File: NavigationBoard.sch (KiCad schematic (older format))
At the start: 13 parts, among them J1 Conn_01x03, J2 Conn_01x03, J3 Conn_01x03, J4 Conn_01x03, U1 ATmega2560-16AU, U2 RFM96W-433S2, U4 MPL115A1, U5 L86

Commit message: remove L86, fix Lora symbol
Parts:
- removed U5: L86, GPS:L86, symbol GPS:L86
- U2: symbol RF_AM_FM:RFM96W-433S2 -> RF_Module:RFM96W-433S2
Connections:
- wire segments 34 -> 27

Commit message: 3V regulator, crystal oscillator, reset switch, new GPS
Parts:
- added C10: 22µF, Capacitor_SMD:C_1206_3216Metric, symbol Device:C
- added C7, C8: 8pF, Capacitor_SMD:C_0603_1608Metric, symbol Device:C_Small
- added C9: 10µF, Capacitor_SMD:C_1210_3225Metric, symbol Device:C
- added R10, R11, R7, R8, R9: 10k, Resistor_SMD:R_0603_1608Metric, symbol Device:R_Small
- added SW1: SW_Push, Button_Switch_SMD:SW_SPST_PTS810, symbol Switch:SW_Push
- added U5: ublox_SAM-M8Q, RF_GPS:ublox_SAM-M8Q, symbol RF_GPS:ublox_SAM-M8Q
- added U6: LMZM23600V3, Package_LGA:Texas_SIL0010A_MicroSiP-10-1EP_3.8x3mm_P0.6mm_EP0.7x2.9mm_ThermalVias, symbol Regulator_Switching:LMZM23600V3
- added Y1: 16MHz, Crystal:Crystal_SMD_5032-2Pin_5.0x3.2mm, symbol Device:Crystal_Small
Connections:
- net labels added: +5V, ~RESET
- wire segments 27 -> 88
- no-connect marks 0 -> 1
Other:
- moved on the sheet: AE1, H1, H2, H3, H4, U1, U2

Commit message: add ISP, MPL3115A2
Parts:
- removed U4: MPL115A1, Package_LGA:NXP_MPL115A1_LGA-8_3x5mm_P1.25mm, symbol Sensor_Pressure:MPL115A1
- added J6: AVR-ISP-6, Connector_IDC:IDC-Header_2x03_P2.54mm_Vertical, symbol Connector:AVR-ISP-6
- added U4: MPL3115A2, Package_LGA:NXP_LGA-8_3x5mm_P1.25mm_H1.1mm, symbol Sensor_Pressure:MPL3115A2
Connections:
- net labels added: +3V3, ~RST
- wire segments 88 -> 94
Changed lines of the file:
@@
-$EndComp
-$Comp
-L Sensor_Pressure:MPL115A1 U4
-U 1 1 5CBD9B8B
-P 9700 4500
-F 0 "U4" H 10244 4546 50  0000 L CNN
-F 1 "MPL115A1" H 10244 4455 50  0000 L CNN
-F 2 "Package_LGA:NXP_MPL115A1_LGA-8_3x5mm_P1.25mm" H 9850 3800 50  0001 C CNN
-F 3 "http://www.nxp.com/assets/documents/data/en/data-sheets/MPL115A1.pdf" H 9700 4500 50  0001 C CNN
-	1    9700 4500
-	1    0    0    -1
 $EndComp
 $Comp
@@
 Wire Wire Line
 	6400 5500 6650 5500
+$Comp
+L Connector:AVR-ISP-6 J6
+U 1 1 5E8952E8
+P 6550 3800
+F 0 "J6" H 6270 3896 50  0000 R CNN
+F 1 "AVR-ISP-6" H 6270 3805 50  0000 R CNN
+F 2 "Connector_IDC:IDC-Header_2x03_P2.54mm_Vertical" V 6300 3850 50  0001 C CNN
+F 3 " ~" H 5275 3250 50  0001 C CNN
+	1    6550 3800
+	-1   0    0    -1
+$EndComp
+Wire Wire Line
+	6150 3600 6100 3600
+Wire Wire Line
+	6150 3700 6100 3700
+Wire Wire Line
+	6150 3800 6100 3800
+Wire Wire Line
+	6150 3900 6100 3900
+Wire Wire Line
+	6650 3300 6650 3200
+Wire Wire Line
+	6650 4200 6650 4300
+$Comp
+L power:GND #PWR0120
+U 1 1 5E8A7489
+P 6650 4300
+F 0 "#PWR0120" H 6650 4050 50  0001 C CNN
+F 1 "GND" H 6655 4127 50  0000 C CNN
+F 2 "" H 6650 4300 50  0001 C CNN
+F 3 "" H 6650 4300 50  0001 C CNN
+	1    6650 4300
+	1    0    0    -1
+$EndComp
+$Comp
+L power:+3V3 #PWR0121
+U 1 1 5E8A80F1
+P 6650 3200
+F 0 "#PWR0121" H 6650 3050 50  0001 C CNN
+F 1 "+3V3" H 6665 3373 50  0000 C CNN
+F 2 "" H 6650 3200 50  0001 C CNN
+F 3 "" H 6650 3200 50  0001 C CNN
+	1    6650 3200
+	1    0    0    -1
+$EndComp
+Text Label 6100 3600 2    50   ~ 0
+MISO
+Text Label 6100 3700 2    50   ~ 0
+MOSI
+Text Label 6100 3800 2    50   ~ 0
+SCK
+Text Label 6100 3900 2    50   ~ 0
+~RST
+$Comp
+L Sensor_Pressure:MPL3115A2 U4
+U 1 1 5E8CB1FC
+P 9650 4500
+F 0 "U4" H 9650 3911 50  0000 C CNN
+F 1 "MPL3115A2" H 9650 3820 50  0000 C CNN
+F 2 "Package_LGA:NXP_LGA-8_3x5mm_P1.25mm_H1.1mm" H 10650 4050 50  0001 C CNN
+F 3 "https://www.nxp.com/docs/en/data-sheet/MPL3115A2.pdf" H 9650 4500 50  0001 C CNN
+	1    9650 4500
+	1    0    0    -1
+$EndComp
 $EndSCHEMATC

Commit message: no clue, this has been >4 months and diff is kinda useless here...
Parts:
- added C11: 10µF, Capacitor_SMD:C_0603_1608Metric, symbol Device:C_Small
- added C12: 100nF, Capacitor_SMD:C_0603_1608Metric, symbol Device:C
- added C13: 100nF, Capacitor_SMD:C_0603_1608Metric, symbol Device:C_Small
- added J7: Conn_01x02, Connector_AMASS:AMASS_XT30UPB-M_1x02_P5.0mm_Vertical, symbol Connector_Generic:Conn_01x02
- added R12, R13: 10k, Resistor_SMD:R_0603_1608Metric, symbol Device:R_Small
- AE1: footprint Connector_Coaxial:MMCX_Molex_73415-0961_Horizontal_1.6mm-PCB -> Connector_Coaxial:SMA_Molex_73251-1153_EdgeMount_Horizontal
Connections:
- net +3V3: now also U4.1 (VDD), U4.4 (VDDIO), C11.2, C13.2, R12.1, R13.1
- net GND: now also C10.2, C9.2, U4.3 (GND), U6.1 (GND), U6.11 (GND), U6.2 (MODE/SYNC), C11.1, C12.1, C13.1
- net SCL: now reaches U1.43 (PD0)
- net SCL: now also U4.8 (SCL), R12.2
- net SDA: now reaches U1.44 (PD1)
- net SDA: now also U4.7 (SDL), R13.2
- net at U4.2 (CAP): now also C12.2
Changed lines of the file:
@@
 F 0 "AE1" H 6294 1989 50  0000 L CNN
 F 1 "Antenna_Shield" H 6294 1898 50  0000 L CNN
-F 2 "Connector_Coaxial:MMCX_Molex_73415-0961_Horizontal_1.6mm-PCB" H 6150 2050 50  0001 C CNN
+F 2 "Connector_Coaxial:SMA_Molex_73251-1153_EdgeMount_Horizontal" H 6150 2050 50  0001 C CNN
 F 3 "~" H 6150 2050 50  0001 C CNN
 	1    6150 1950
@@
 U 1 1 5CBDAC91
 P 5500 2500
-F 0 "U2" H 5500 3181 50  0000 C CNN
-F 1 "RFM96W-433S2" H 5500 3090 50  0000 C CNN
+F 0 "U2" H 5200 3000 50  0000 C CNN
+F 1 "RFM96W-433S2" H 5800 2950 50  0000 C CNN
 F 2 "RF_Module:HOPERF_RFM9XW_SMD" H 2200 4150 50  0001 C CNN
 F 3 "http://www.hoperf.com/upload/rf/RFM95_96_97_98W.pdf" H 2200 4150 50  0001 C CNN
@@
 U 1 1 5E8952E8
 P 6550 3800
-F 0 "J6" H 6270 3896 50  0000 R CNN
-F 1 "AVR-ISP-6" H 6270 3805 50  0000 R CNN
+F 0 "J6" H 6350 3450 50  0000 R CNN
+F 1 "AVR-ISP-6" H 7000 3450 50  0000 R CNN
 F 2 "Connector_IDC:IDC-Header_2x03_P2.54mm_Vertical" V 6300 3850 50  0001 C CNN
 F 3 " ~" H 5275 3250 50  0001 C CNN
@@
 U 1 1 5E8CB1FC
 P 9650 4500
-F 0 "U4" H 9650 3911 50  0000 C CNN
-F 1 "MPL3115A2" H 9650 3820 50  0000 C CNN
+F 0 "U4" H 9400 4050 50  0000 C CNN
+F 1 "MPL3115A2" H 10000 4050 50  0000 C CNN
 F 2 "Package_LGA:NXP_LGA-8_3x5mm_P1.25mm_H1.1mm" H 10650 4050 50  0001 C CNN
 F 3 "https://www.nxp.com/docs/en/data-sheet/MPL3115A2.pdf" H 9650 4500 50  0001 C CNN
@@
 	1    0    0    -1
 $EndComp
+Text Label 4650 3900 0    50   ~ 0
+SCL
+Text Label 4650 4000 0    50   ~ 0
+SDA
+$Comp
+L Device:R_Small R12
+U 1 1 5E8D9BD0
+P 4850 3700
+F 0 "R12" V 4850 3700 50  0000 C CNN
+F 1 "10k" V 4750 3700 50  0000 C CNN
+F 2 "Resistor_SMD:R_0603_1608Metric" H 4850 3700 50  0001 C CNN
+F 3 "~" H 4850 3700 50  0001 C CNN
+	1    4850 3700
+	1    0    0    -1
+$EndComp
+$Comp
+L Device:R_Small R13
+U 1 1 5E8D9BD6
+P 5000 3700
+F 0 "R13" V 5000 3700 50  0000 C CNN
+F 1 "10k" H 5059 3745 50  0001 L CNN
+F 2 "Resistor_SMD:R_0603_1608Metric" H 5000 3700 50  0001 C CNN
+F 3 "~" H 5000 3700 50  0001 C CNN
+	1    5000 3700
+	1    0    0    -1
+$EndComp
+$Comp
+L power:+3.3V #PWR0122
+U 1 1 5E8D9BDC
+P 4850 3500
+F 0 "#PWR0122" H 4850 3350 50  0001 C CNN
+F 1 "+3.3V" H 4865 3673 50  0000 C CNN
+F 2 "" H 4850 3500 50  0001 C CNN
+F 3 "" H 4850 3500 50  0001 C CNN
+	1    4850 3500
+	1    0    0    -1
+$EndComp
+Wire Wire Line
+	4850 3500 4850 3550
+Wire Wire Line
+	5000 3600 5000 3550
+Wire Wire Line
+	5000 3550 4850 3550
+Connection ~ 4850 3550
+Wire Wire Line
+	4850 3550 4850 3600
+Wire Wire Line
+	4850 3900 4850 3800
+Wire Wire Line
+	4550 3900 4850 3900
+Wire Wire Line
+	5000 4000 5000 3800
+Wire Wire Line
+	4550 4000 5000 4000
+Wire Wire Line
+	9250 4500 9150 4500
+Wire Wire Line
+	9250 4400 9150 4400
+Text Label 9150 4400 2    50   ~ 0
+SDA
+Text Label 9150 4500 2    50   ~ 0
+SCL
+Wire Wire Line
+	9550 4000 9550 3950
+Wire Wire Line
+	9550 3950 9650 3950
+Wire Wire Line
+	9650 3950 9650 4000
+Connection ~ 9550 3950
+Wire Wire Line
+	9550 3950 9550 3900
+$Comp
+L power:+3V3 #PWR0123
+U 1 1 5E8EE8BA
+P 9550 3900
+F 0 "#PWR0123" H 9550 3750 50  0001 C CNN
+F 1 "+3V3" H 9565 4073 50  0000 C CNN
+F 2 "" H 9550 3900 50  0001 C CNN
+F 3 "" H 9550 3900 50  0001 C CNN
+	1    9550 3900
+	1    0    0    -1
+$EndComp
+$Comp
+L power:GND #PWR0124
+U 1 1 5E8F05AB
+P 7200 5600
+F 0 "#PWR0124" H 7200 5350 50  0001 C CNN
+F 1 "GND" H 7205 5427 50  0000 C CNN
+F 2 "" H 7200 5600 50  0001 C CNN
+F 3 "" H 7200 5600 50  0001 C CNN
+	1    7200 5600
+	1    0    0    -1
+$EndComp
+Wire Wire Line
+	7200 5600 7200 5500
+$Comp
+L power:GND #PWR0125
+U 1 1 5E8F3C9C
+P 9650 5100
+F 0 "#PWR0125" H 9650 4850 50  0001 C CNN
+F 1 "GND" H 9655 4927 50  0000 C CNN
+F 2 "" H 9650 5100 50  0001 C CNN
+F 3 "" H 9650 5100 50  0001 C CNN
+	1    9650 5100
+	1    0    0    -1
+$EndComp
+Wire Wire Line
+	9650 5100 9650 5000
+$Comp
+L Device:C C12
+U 1 1 5E8F7F8C
+P 10300 4700
+F 0 "C12" V 10048 4700 50  0000 C CNN
+F 1 "100nF" V 10139 4700 50  0000 C CNN
+F 2 "Capacitor_SMD:C_0603_1608Metric" H 10338 4550 50  0001 C CNN
+F 3 "~" H 10300 4700 50  0001 C CNN
+	1    10300 4700
+	0    1    1    0
+$EndComp
+Wire Wire Line
+	10450 4700 10550 4700
+Wire Wire Line
+	10550 4700 10550 4800
+$Comp
+L power:GND #PWR0126
+U 1 1 5E8FB81C
+P 10550 4800
+F 0 "#PWR0126" H 10550 4550 50  0001 C CNN
+F 1 "GND" H 10555 4627 50  0000 C CNN
+F 2 "" H 10550 4800 50  0001 C CNN
+F 3 "" H 10550 4800 50  0001 C CNN
+	1    10550 4800
+	1    0    0    -1
+$EndComp
+Wire Wire Line
+	10150 4700 10050 4700
+$Comp
+L Device:C_Small C13
+U 1 1 5E8FF505
+P 10550 4100
+F 0 "C13" H 10458 4054 50  0000 R CNN
+F 1 "100nF" H 10458 4145 50  0000 R CNN
+F 2 "Capacitor_SMD:C_0603_1608Metric" H 10550 4100 50  0001 C CNN
+F 3 "~" H 10550 4100 50  0001 C CNN
+	1    10550 4100
+	-1   0    0    1
+$EndComp
+$Comp
+L Device:C_Small C11
+U 1 1 5E9000AF
+P 10200 4100
+F 0 "C11" H 10108 4054 50  0000 R CNN
+F 1 "10µF" H 10108 4145 50  0000 R CNN
+F 2 "Capacitor_SMD:C_0603_1608Metric" H 10200 4100 50  0001 C CNN
+F 3 "~" H 10200 4100 50  0001 C CNN
+	1    10200 4100
+	-1   0    0    1
+$EndComp
+Connection ~ 9650 3950
+Wire Wire Line
+	10200 4000 10200 3950
+Wire Wire Line
+	10200 3950 9650 3950
+Wire Wire Line
+	10200 4200 10200 4250
+Wire Wire Line
+	10200 4250 10550 4250
+Wire Wire Line
+	10550 4700 10550 4250
+Connection ~ 10550 4700
+Wire Wire Line
+	10550 4200 10550 4250
+Connection ~ 10550 4250
+Wire Wire Line
+	10200 3950 10550 3950
+Wire Wire Line
+	10550 3950 10550 4000
+Connection ~ 10200 3950
+$Comp
+L Connector_Generic:Conn_01x02 J7
+U 1 1 5E831A29
+P 8450 2750
+F 0 "J7" H 8530 2742 50  0000 L CNN
+F 1 "Conn_01x02" H 8530 2651 50  0000 L CNN
+F 2 "Connector_AMASS:AMASS_XT30UPB-M_1x02_P5.0mm_Vertical" H 8450 2750 50  0001 C CNN
+F 3 "~" H 8450 2750 50  0001 C CNN
+	1    8450 2750
+	1    0    0    -1
+$EndComp

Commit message: Erster Grober Entwurf
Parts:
- U4: symbol Sensor_Pressure:MPL3115A2 -> NavigationBoard-rescue:MPL3115A2-Sensor_Pressure
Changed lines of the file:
@@
 ~RST
 $Comp
-L Sensor_Pressure:MPL3115A2 U4
+L NavigationBoard-rescue:MPL3115A2-Sensor_Pressure U4
 U 1 1 5E8CB1FC
 P 9650 4500

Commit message: Kleinerer AVR-ISP Stecker
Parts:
- J6: footprint Connector_IDC:IDC-Header_2x03_P2.54mm_Vertical -> Connector_PinHeader_2.54mm:PinHeader_2x03_P2.54mm_Vertical
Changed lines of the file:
@@
 F 0 "J6" H 6350 3450 50  0000 R CNN
 F 1 "AVR-ISP-6" H 7000 3450 50  0000 R CNN
-F 2 "Connector_IDC:IDC-Header_2x03_P2.54mm_Vertical" V 6300 3850 50  0001 C CNN
+F 2 "Connector_PinHeader_2.54mm:PinHeader_2x03_P2.54mm_Vertical" V 6300 3850 50  0001 C CNN
 F 3 " ~" H 5275 3250 50  0001 C CNN
 	1    6550 3800

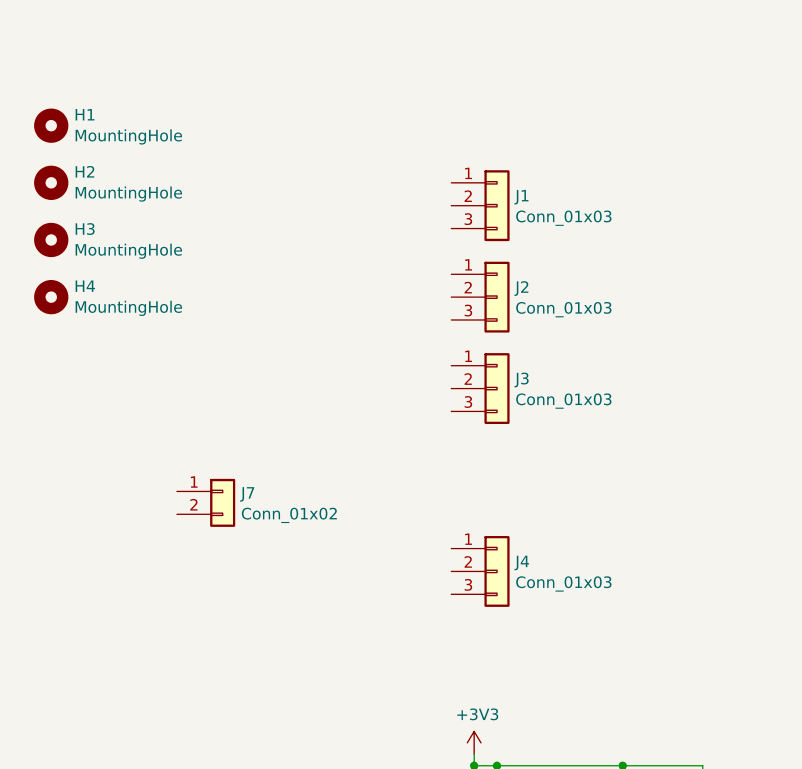
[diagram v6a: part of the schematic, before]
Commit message: XT 30 entfernt
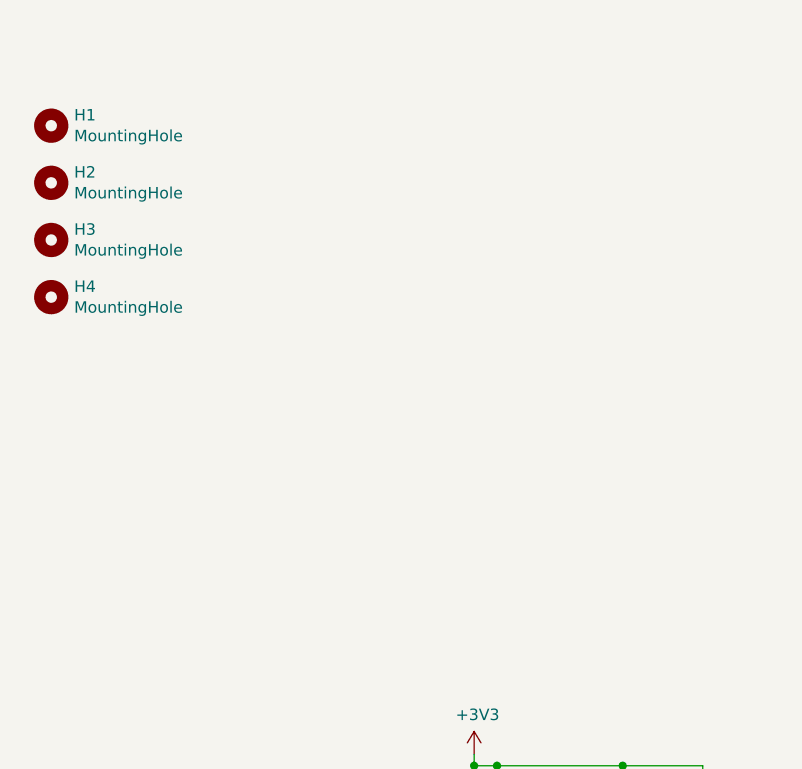
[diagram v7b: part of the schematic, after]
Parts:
- removed J1, J2, J3, J4: Conn_01x03, Connector_PinHeader_2.54mm:PinHeader_1x03_P2.54mm_Vertical, symbol Connector_Generic:Conn_01x03
- removed J7: Conn_01x02, Connector_AMASS:AMASS_XT30UPB-M_1x02_P5.0mm_Vertical, symbol Connector_Generic:Conn_01x02
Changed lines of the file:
@@
-$EndComp
-$Comp
-L Connector_Generic:Conn_01x03 J1
-U 1 1 5CBD6E70
-P 9650 1500
-F 0 "J1" H 9730 1542 50  0000 L CNN
-F 1 "Conn_01x03" H 9730 1451 50  0000 L CNN
-F 2 "Connector_PinHeader_2.54mm:PinHeader_1x03_P2.54mm_Vertical" H 9650 1500 50  0001 C CNN
-F 3 "~" H 9650 1500 50  0001 C CNN
-	1    9650 1500
-	1    0    0    -1
-$EndComp
-$Comp
-L Connector_Generic:Conn_01x03 J2
-U 1 1 5CBD7518
-P 9650 1900
-F 0 "J2" H 9730 1942 50  0000 L CNN
-F 1 "Conn_01x03" H 9730 1851 50  0000 L CNN
-F 2 "Connector_PinHeader_2.54mm:PinHeader_1x03_P2.54mm_Vertical" H 9650 1900 50  0001 C CNN
-F 3 "~" H 9650 1900 50  0001 C CNN
-	1    9650 1900
-	1    0    0    -1
-$EndComp
-$Comp
-L Connector_Generic:Conn_01x03 J3
-U 1 1 5CBD7CD8
-P 9650 2300
-F 0 "J3" H 9730 2342 50  0000 L CNN
-F 1 "Conn_01x03" H 9730 2251 50  0000 L CNN
-F 2 "Connector_PinHeader_2.54mm:PinHeader_1x03_P2.54mm_Vertical" H 9650 2300 50  0001 C CNN
-F 3 "~" H 9650 2300 50  0001 C CNN
-	1    9650 2300
-	1    0    0    -1
-$EndComp
-$Comp
-L Connector_Generic:Conn_01x03 J4
-U 1 1 5CBD902F
-P 9650 3100
-F 0 "J4" H 9730 3142 50  0000 L CNN
-F 1 "Conn_01x03" H 9730 3051 50  0000 L CNN
-F 2 "Connector_PinHeader_2.54mm:PinHeader_1x03_P2.54mm_Vertical" H 9650 3100 50  0001 C CNN
-F 3 "~" H 9650 3100 50  0001 C CNN
-	1    9650 3100
-	1    0    0    -1
 $EndComp
 $Comp
@@
 	10550 3950 10550 4000
 Connection ~ 10200 3950
-$Comp
-L Connector_Generic:Conn_01x02 J7
-U 1 1 5E831A29
-P 8450 2750
-F 0 "J7" H 8530 2742 50  0000 L CNN
-F 1 "Conn_01x02" H 8530 2651 50  0000 L CNN
-F 2 "Connector_AMASS:AMASS_XT30UPB-M_1x02_P5.0mm_Vertical" H 8450 2750 50  0001 C CNN
-F 3 "~" H 8450 2750 50  0001 C CNN
-	1    8450 2750
-	1    0    0    -1
-$EndComp
 $EndSCHEMATC
